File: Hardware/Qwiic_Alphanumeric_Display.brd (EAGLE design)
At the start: 40.6 x 27.9 mm, 45 parts, among them J4 Vertical Qwiic Connector, J5 Vertical Qwiic Connector

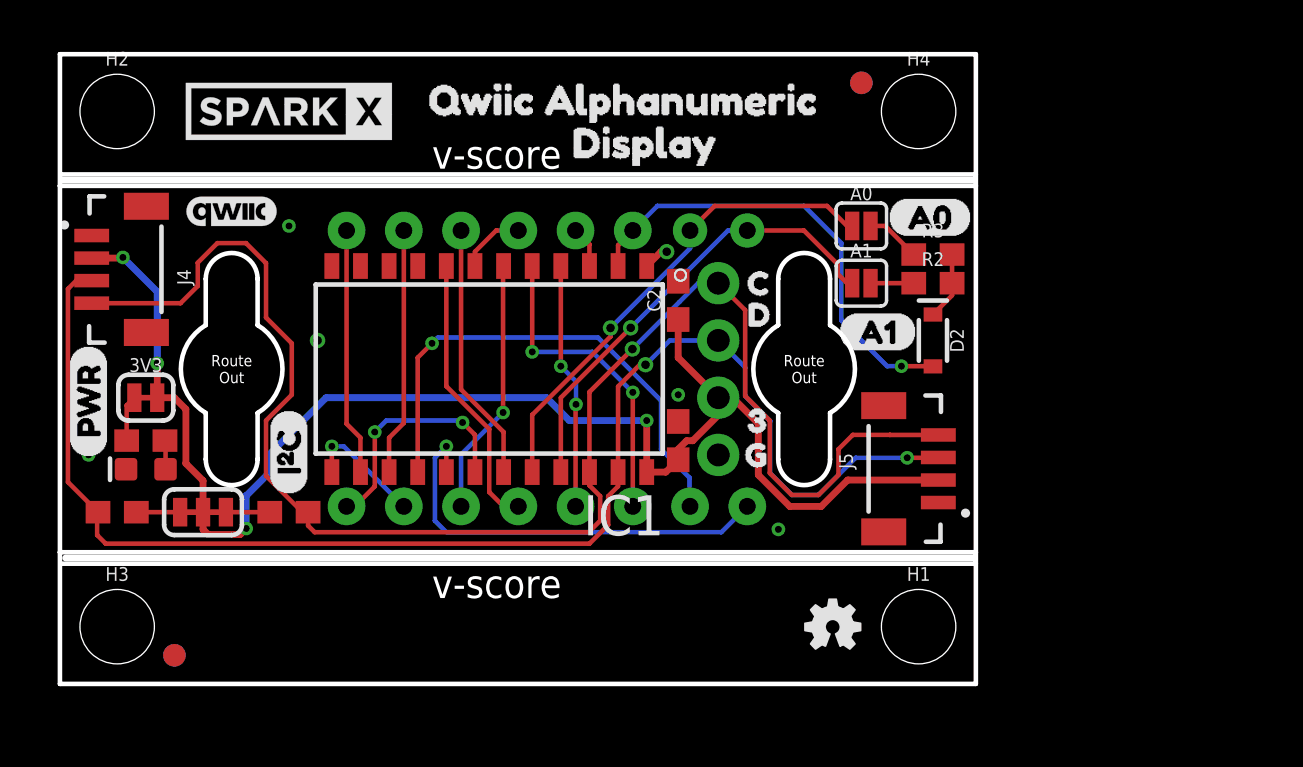
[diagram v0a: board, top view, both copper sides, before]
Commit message: Update design for protos
Add 5V boost circuit for ht16k33
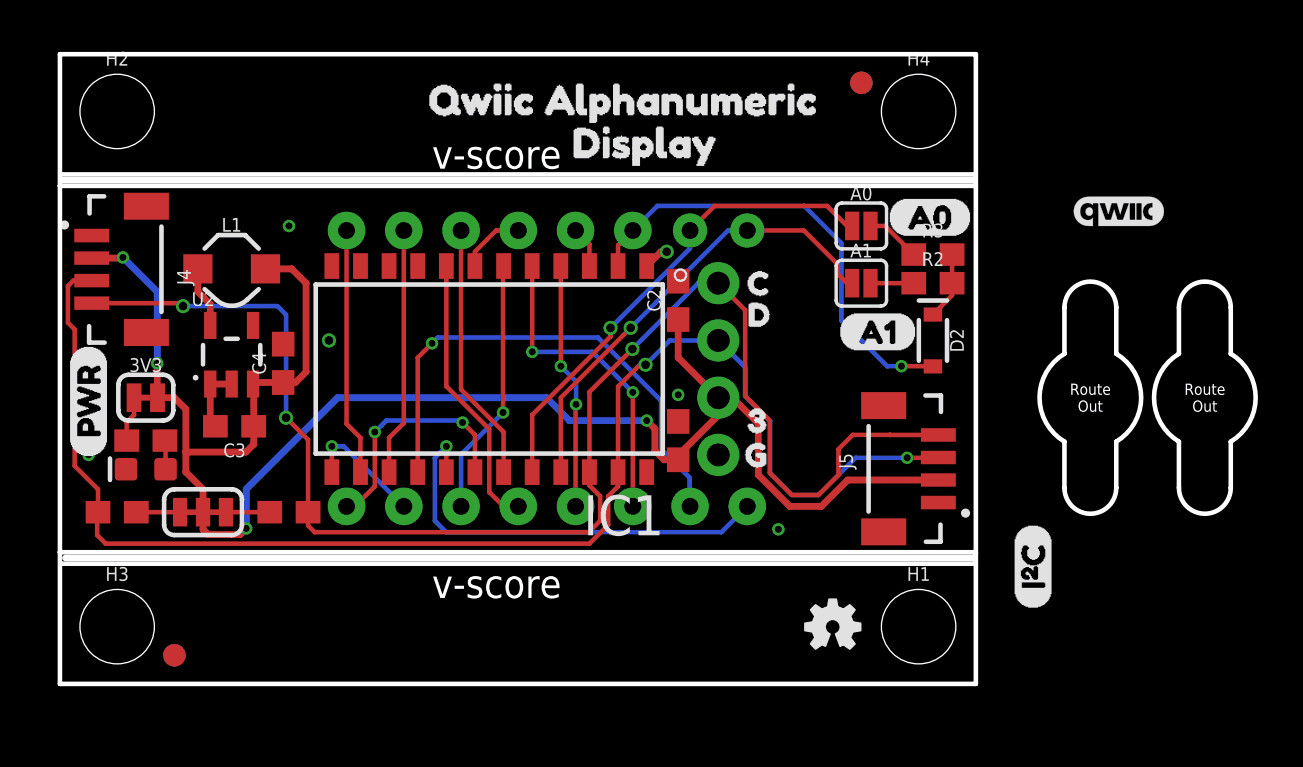
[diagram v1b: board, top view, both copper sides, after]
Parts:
- removed U$7, U$8: SPARKX-LOGO4, SparkX:SPARKX-MEDIUM
- added C3: 4.7uF, SparkFun-Capacitors:0603
- added C4: 10uF, SparkFun-Capacitors:0603
- added L1: 4.7µH/±30%/1.2A, SparkFun-Coils:INDUCTOR_4.7UH
- added U2: XC9140, SparkFun-IC-Power:SOT23-5
- moved U$6 39.4 mm to (47.0, 22.2)
- moved U$19 38.1 mm to (45.7, 14.0)
- moved U$10 33.4 mm to (43.2, 4.57)
- moved U$18 17.8 mm to (50.8, 14.0)
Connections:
- new net 5V: IC1.24
- new net N$10: L1.P$1, U2.5
- new net N$11: U2.4
- net 3.3V: now also C3.1, C4.1, L1.P$2, U2.3; no longer IC1.24
- net GND: now also C3.2, C4.2, U2.1, U2.2
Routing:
- net 3.3V: track 64.8 -> 77.5 mm
- net SCL: track 69.3 -> 64.5 mm, vias 1 -> 3
- net GND: track 1.15 -> 4.07 mm
- net N$10: track 0.00 -> 2.74 mm

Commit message: Run schematic/board autochecklist
Update font to vector
Make sure all parts (except for new ones) are in SF Eagle libs
Add measures
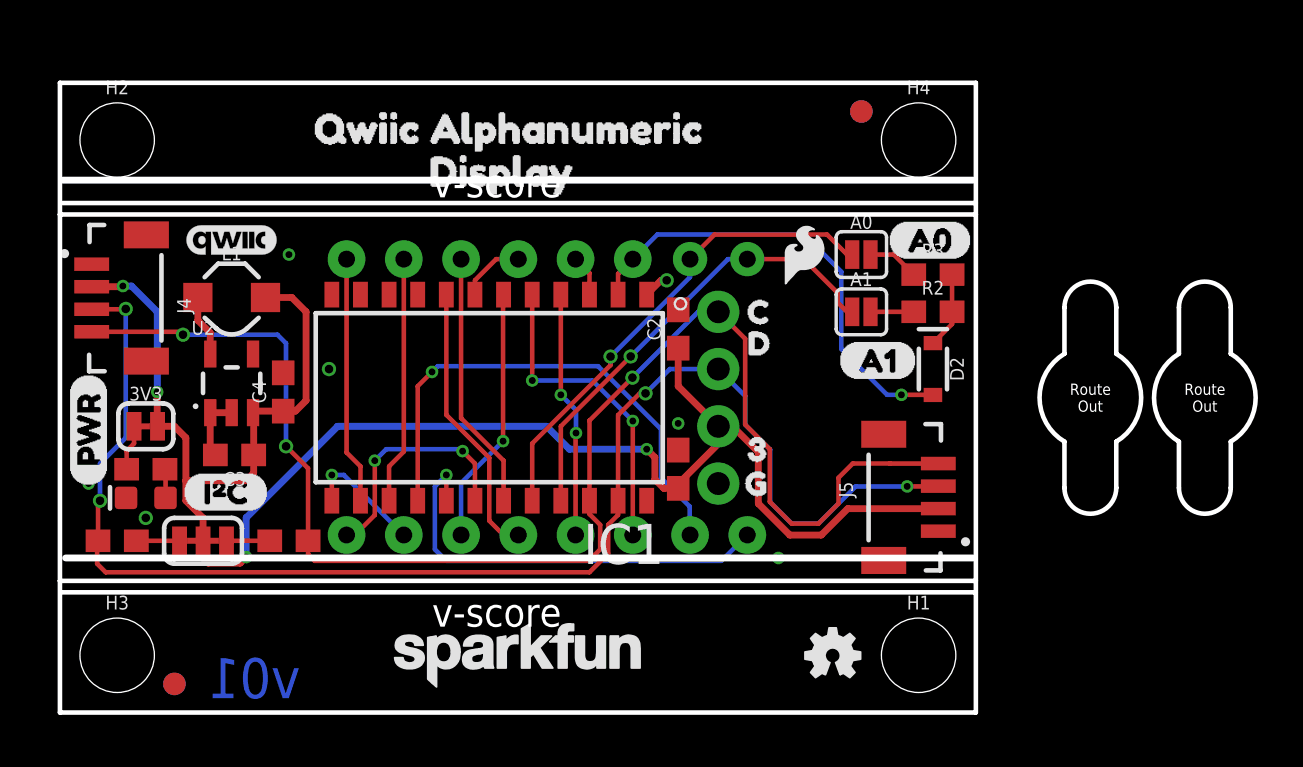
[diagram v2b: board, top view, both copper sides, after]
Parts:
- added LOGO2, LOGO3: SFE_LOGO_NAME.1_INCH, SparkFun-Aesthetics:SFE_LOGO_NAME_.1
- added LOGO4: SFE_LOGO_FLAME.1_INCH, SparkFun-Aesthetics:SFE_LOGO_FLAME_.1
- L1: value 4.7µH/±30%/1.2A -> 4.7µH
- moved U$6 39.4 mm to (7.62, 21.0)
- moved U$10 38.1 mm to (5.46, 9.78), turned to 0 degrees
- moved U$16 6.48 mm to (15.2, 24.0)
- moved U$17 5.70 mm to (24.0, 24.1)
- moved U$15 5.24 mm to (10.2, 25.9)
- moved U$13 5.24 mm to (29.7, 25.9)
- moved H2 1.27 mm to (2.54, 25.4)
- moved H4 1.27 mm to (38.1, 25.4)
- moved 3V3 1.27 mm to (3.81, 12.7)
- moved D2 1.27 mm to (38.7, 15.2)
- moved U$1 1.27 mm to (29.6, 11.7)
- moved U$3 1.27 mm to (1.27, 10.0)
- moved I2C 1.27 mm to (6.35, 7.62)
- moved R4 1.27 mm to (2.54, 7.62)
- moved R5 1.27 mm to (10.2, 7.62)
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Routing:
- net SDA: track 63.0 -> 63.5 mm, vias 2 -> 4
- net GND: vias 6 -> 7
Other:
- outline, holes or cut-outs redrawn
- board text added: "All measures in inches"
- board text added: "Priyanka Makin"
- board text added: "v01"
- board text removed: "Madison Chodikov"

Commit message: Updates after proto review
Update HT16K33 to VK16K33
Compared datasheets, it’s a drop in replacement!
Removed PWR LED and jumper
5V net now connects to the LED driver IC
New mounting hole design
I2C pullups became 4.7k and removed jumper
You can only connect up to 4 displays on one bus
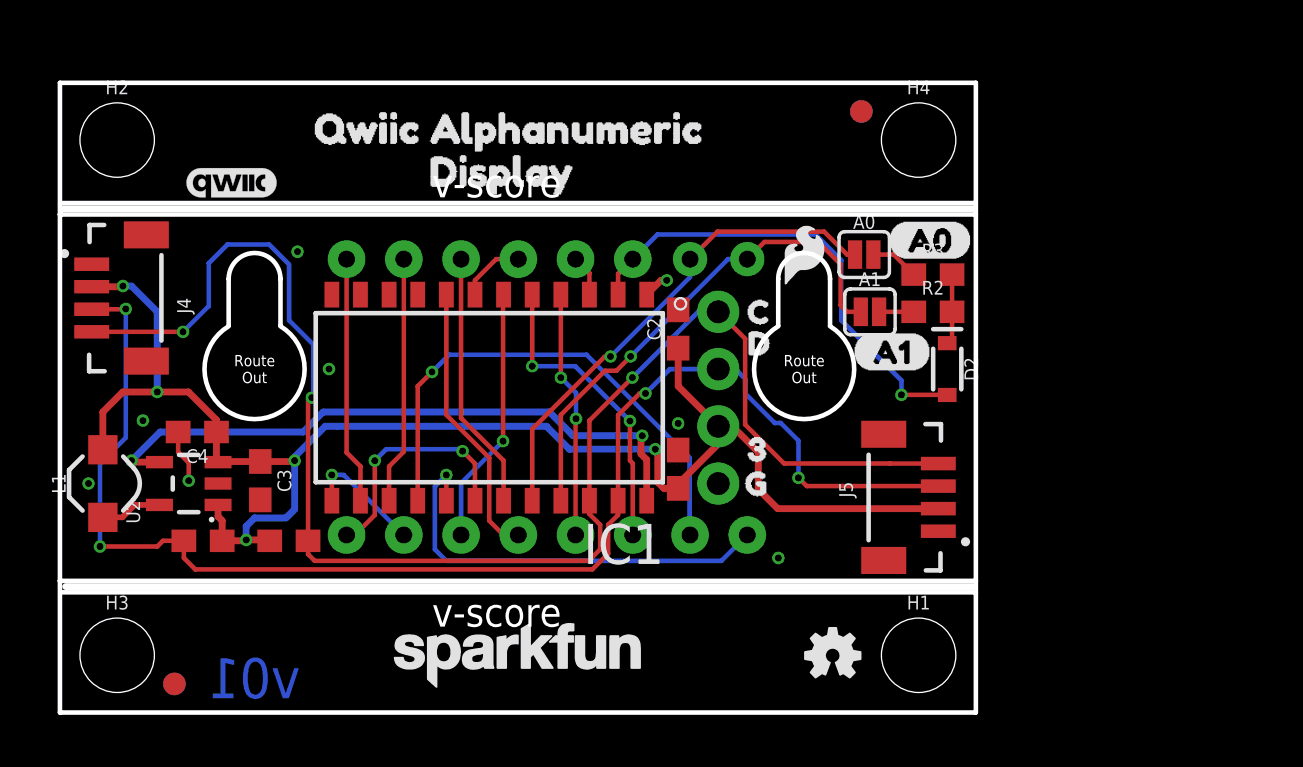
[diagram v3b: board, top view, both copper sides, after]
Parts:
- removed 3V3: JUMPER-SMT_2_NC_TRACE_SILK, SparkFun-Jumpers:SMT-JUMPER_2_NC_TRACE_SILK
- removed D1: RED, SparkFun-LED:LED-0603
- removed I2C: JUMPER-SMT_3_2-NC_TRACE_SILK, SparkFun-Jumpers:SMT-JUMPER_3_2-NC_TRACE_SILK
- removed R1: 1k, SparkFun-Resistors:0603
- removed U$10: (no value), Labels:I_SUPER2_C-()-04
- removed U$18, U$19: MOUNTING_HOLE_M2-0.4X6, Alphanumeric_Display_Library:MOUNTING_HOLE_M2-0.4X6
- added U$7: MOUNTING_HOLE_M2-0.4X6, Alphanumeric_Display_Library:MOUNTING_HOLE_M2-0.4X6
- IC1: device Alphanumeric_Display_Library:HT16K33 -> Alphanumeric_Display_Library:VK16K33
- R4, R5: value 2.2k -> 4.7k
- U$3: value (none) -> MOUNTING_HOLE_M2-0.4X6; device buzzard_labels:PWR5 -> Alphanumeric_Display_Library:MOUNTING_HOLE_M2-0.4X6
- moved U$3 32.2 mm to (33.0, 15.2), turned to 0 degrees
- moved L1 10.0 mm to (1.91, 10.2), turned to 90 degrees
- moved U2 4.84 mm to (5.71, 10.2), turned to 90 degrees
- moved C4 4.20 mm to (6.10, 12.4), turned to 180 degrees
- moved R4 3.81 mm to (6.35, 7.62)
- moved U$6 2.54 mm to (7.62, 23.5)
- moved C3 1.62 mm to (8.89, 10.3), turned to 270 degrees
- moved U$21 0.74 mm to (35.2, 16.0)
- moved D2 0.63 mm to (39.4, 15.2)
- moved A1 0.38 mm to (35.9, 17.8)
- moved A0 0.13 mm to (35.7, 20.3)
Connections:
- removed net N$1: D1.A, R1.1
- removed net N$11: U2.4
- removed net N$4: I2C.1, R5.2
- removed net N$5: I2C.3, R4.2
- removed net N$7: 3V3.1, R1.2
- net 3.3V: now also R4.2, R5.2, U2.1; no longer 3V3.2, I2C.2
- net 5V: now also U2.4
- net GND: no longer D1.C, U2.1
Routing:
- net 5V: track 0.00 -> 28.3 mm, vias 0 -> 2
- net 3.3V: track 77.7 -> 68.5 mm, vias 4 -> 5
- net SCL: track 64.5 -> 67.0 mm
- net SDA: track 63.5 -> 61.3 mm
- net DIG_1A: track 20.5 -> 22.6 mm
- net N$7: track 2.04 -> 0.00 mm
- net N$4: track 1.92 -> 0.00 mm
- net N$5: track 1.92 -> 0.00 mm
- net N$1: track 1.28 -> 0.00 mm
- net GND: track 4.07 -> 3.51 mm, vias 7 -> 8
- net COM_A: track 20.6 -> 21.1 mm
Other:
- outline, holes or cut-outs redrawn

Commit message: Re-generate buzzard labels
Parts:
- removed U$1: (no value), buzzard_labels (65):32
- removed U$2: (no value), buzzard_labels (65):C0
- removed U$20: (no value), buzzard_labels (63):A00
- removed U$21: (no value), buzzard_labels (63):A11
- removed U$4: (no value), buzzard_labels (65):D1
- removed U$5: (no value), buzzard_labels (65):G3
- added U$10, U$11: (no value), output:DISPLAY0
- added U$12: (no value), output:#A0#0
- added U$14: (no value), output:C0
- added U$8, U$9: (no value), output:QWIIC_ALPHANUMERIC0
- U$13: device buzzard_labels (4):QWIIC_ALPHANUMERIC0 -> output:#A1#0
- U$15: device buzzard_labels (4):QWIIC_ALPHANUMERIC0 -> output:D0
- U$16: device buzzard_labels (4):DISPLAY1 -> output:30
- U$17: device buzzard_labels (4):DISPLAY1 -> output:G0
- moved U$15 21.4 mm to (29.7, 17.1)
- moved U$16 18.4 mm to (29.7, 12.7)
- moved U$17 15.1 mm to (29.7, 10.2), flipped to the top
- moved LOGO4 12.8 mm to (34.3, 7.62)
- moved U$13 11.5 mm to (35.3, 15.9), flipped to the top
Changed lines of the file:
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@@
 <?xml version="1.0" encoding="utf-8"?>
 <!DOCTYPE eagle SYSTEM "eagle.dtd">
-<eagle version="9.5.2">
+<eagle version="9.6.2">
 <drawing>
 <settings>
@@
 <attribute name="PROD_ID" value="RES-07857" x="-41.91" y="72.39" size="1.778" layer="27" rot="R180" display="off"/>
 </element>
-<element name="U$15" library="buzzard_labels (4)" package="QWIIC_ALPHANUMERIC0" value="" x="10.16" y="25.908" smashed="yes"/>
-<element name="U$16" library="buzzard_labels (4)" package="DISPLAY1" value="" x="15.24" y="24.003" smashed="yes"/>
-<element name="U$13" library="buzzard_labels (4)" package="QWIIC_ALPHANUMERIC0" value="" x="29.718" y="25.908" smashed="yes" rot="MR0"/>
-<element name="U$17" library="buzzard_labels (4)" package="DISPLAY1" value="" x="24.003" y="24.13" smashed="yes" rot="MR0"/>
 <element name="A1" library="SparkFun-Jumpers" package="SMT-JUMPER_2_NO_SILK" package3d_urn="urn:adsk.eagle:package:39279/1" value="JUMPER-SMT_2_NO_SILK" x="35.941" y="17.78" smashed="yes">
 <attribute name="NAME" x="35.941" y="18.923" size="0.6096" layer="25" font="vector" ratio="20" align="bottom-center"/>
@@
 <attribute name="VALUE" x="26.75" y="21.37" size="1.778" layer="27" rot="R180"/>
 </element>
-<element name="U$20" library="buzzard_labels (63)" package="A00" value="" x="36.703" y="20.955" smashed="yes"/>
-<element name="U$21" library="buzzard_labels (63)" package="A11" value="" x="35.179" y="16.002" smashed="yes"/>
 <element name="U$6" library="SparkFun-Aesthetics" package="QWIIC_4MM" value="" x="7.62" y="23.495" smashed="yes"/>
-<element name="U$1" library="buzzard_labels (65)" package="32" value="" x="29.591" y="11.684" smashed="yes"/>
-<element name="U$2" library="buzzard_labels (65)" package="C0" value="" x="29.591" y="17.78" smashed="yes"/>
-<element name="U$4" library="buzzard_labels (65)" package="D1" value="" x="29.591" y="16.383" smashed="yes"/>
-<element name="U$5" library="buzzard_labels (65)" package="G3" value="" x="29.464" y="10.16" smashed="yes"/>
 <element name="H3" library="SparkFun-Hardware" package="STAND-OFF" value="STAND-OFF" x="2.54" y="2.54" smashed="yes">
 <attribute name="NAME" x="2.54" y="4.572" size="0.6096" layer="25" font="vector" ratio="20" align="bottom-center"/>
@@
 <element name="LOGO2" library="SparkFun-Aesthetics" package="SFE_LOGO_NAME_.1" value="SFE_LOGO_NAME.1_INCH" x="20.32" y="2.54" smashed="yes" rot="MR0"/>
 <element name="LOGO3" library="SparkFun-Aesthetics" package="SFE_LOGO_NAME_.1" value="SFE_LOGO_NAME.1_INCH" x="20.32" y="2.54" smashed="yes"/>
-<element name="LOGO4" library="SparkFun-Aesthetics" package="SFE_LOGO_FLAME_.1" value="SFE_LOGO_FLAME.1_INCH" x="33.02" y="20.32" smashed="yes"/>
+<element name="LOGO4" library="SparkFun-Aesthetics" package="SFE_LOGO_FLAME_.1" value="SFE_LOGO_FLAME.1_INCH" x="34.29" y="7.62" smashed="yes"/>
 <element name="U$3" library="Alphanumeric_Display_Library" package="MOUNTING_HOLE_M2-0.4X6" value="MOUNTING_HOLE_M2-0.4X6" x="33.02" y="15.24" smashed="yes"/>
 <element name="U$7" library="Alphanumeric_Display_Library" package="MOUNTING_HOLE_M2-0.4X6" value="MOUNTING_HOLE_M2-0.4X6" x="8.636" y="15.24" smashed="yes"/>
+<element name="U$8" library="output" package="QWIIC_ALPHANUMERIC0" value="" x="6.604" y="26.289" smashed="yes"/>
+<element name="U$9" library="output" package="QWIIC_ALPHANUMERIC0" value="" x="34.29" y="26.289" smashed="yes" rot="MR0"/>
+<element name="U$10" library="output" package="DISPLAY0" value="" x="14.478" y="24.13" smashed="yes"/>
+<element name="U$11" library="output" package="DISPLAY0" value="" x="26.162" y="24.13" smashed="yes" rot="MR0"/>
+<element name="U$12" library="output" package="#A0#0" value="" x="36.957" y="20.828" smashed="yes"/>
+<element name="U$13" library="output" package="#A1#0" value="" x="35.306" y="15.875" smashed="yes"/>
+<element name="U$14" library="output" package="C0" value="" x="29.718" y="18.669" smashed="yes"/>
+<element name="U$15" library="output" package="D0" value="" x="29.718" y="17.145" smashed="yes"/>
+<element name="U$16" library="output" package="30" value="" x="29.718" y="12.7" smashed="yes"/>
+<element name="U$17" library="output" package="G0" value="" x="29.718" y="10.16" smashed="yes"/>
 </elements>
 <signals>

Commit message: Run checklist
Add voltage ranges on schematic
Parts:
- moved U$6 1.27 mm to (6.35, 23.5)
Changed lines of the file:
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@@
 <?xml version="1.0" encoding="utf-8"?>
 <!DOCTYPE eagle SYSTEM "eagle.dtd">
-<eagle version="9.6.2">
+<eagle version="9.5.2">
 <drawing>
 <settings>
@@
 <attribute name="VALUE" x="26.75" y="21.37" size="1.778" layer="27" rot="R180"/>
 </element>
-<element name="U$6" library="SparkFun-Aesthetics" package="QWIIC_4MM" value="" x="7.62" y="23.495" smashed="yes"/>
+<element name="U$6" library="SparkFun-Aesthetics" package="QWIIC_4MM" value="" x="6.35" y="23.495" smashed="yes"/>
 <element name="H3" library="SparkFun-Hardware" package="STAND-OFF" value="STAND-OFF" x="2.54" y="2.54" smashed="yes">
 <attribute name="NAME" x="2.54" y="4.572" size="0.6096" layer="25" font="vector" ratio="20" align="bottom-center"/>
